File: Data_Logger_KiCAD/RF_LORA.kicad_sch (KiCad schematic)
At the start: 14 parts, among them U3 SX1262IMLTRT, U4 MASW-007221, Y2 Crystal_GND23

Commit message: Sub-schematics Generated
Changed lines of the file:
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@@
+	)
+	(junction
+		(at 83.82 38.1)
+		(diameter 0)
+		(color 0 0 0 0)
 	)
 	(junction
@@
 	(wire
 		(pts
+			(xy 83.82 29.21) (xy 83.82 38.1)
+		)
+		(stroke
+			(width 0)
+			(type default)
+		)
+	)
+	(wire
+		(pts
 			(xy 116.84 69.85) (xy 116.84 76.2)
 		)
@@
 	(wire
 		(pts
+			(xy 77.47 38.1) (xy 83.82 38.1)
+		)
+		(stroke
+			(width 0)
+			(type default)
+		)
+	)
+	(wire
+		(pts
 			(xy 71.12 104.14) (xy 83.82 104.14)
 		)
@@
 	(wire
 		(pts
-			(xy 96.52 38.1) (xy 77.47 38.1)
+			(xy 96.52 38.1) (xy 83.82 38.1)
 		)
 		(stroke
@@
 					(unit 1)
 				)
+			)
+		)
+	)
+	(symbol
+		(lib_id "power:VDDA")
+		(at 83.82 29.21 0)
+		(unit 1)
+		(exclude_from_sim no)
+		(in_bom yes)
+		(on_board yes)
+		(dnp no)
+		(fields_autoplaced yes)
+		(property "Reference" "#PWR024"
+			(at 83.82 33.02 0)
+			(effects
+				(font
+					(size 1.27 1.27)
+				)
+				(hide yes)
+			)
+		)
+		(property "Value" "VDD_Radio"
+			(at 83.82 25.4 0)
+			(effects
+				(font
+					(size 1.27 1.27)
+				)
+			)
+		)
+		(property "Footprint" ""
+			(at 83.82 29.21 0)
+			(effects
+				(font
+					(size 1.27 1.27)
+				)
+				(hide yes)
+			)
+		)
+		(property "Datasheet" ""
+			(at 83.82 29.21 0)
+			(effects
+				(font
+					(size 1.27 1.27)
+				)
+				(hide yes)
+			)
+		)
+		(property "Description" "Power symbol creates a global label with name \"VDDA\""
+			(at 83.82 29.21 0)
+			(effects
+				(font
+					(size 1.27 1.27)
+				)
+				(hide yes)
+			)
+		)
+		(pin "1"
+		)
+		(instances
+			(project ""
+				(path "/db968e42-3ace-4cc9-9096-9d8f48135c40/f67abaa3-07d9-44aa-9d82-6b11f8890146"
+					(reference "#PWR024")
+					(unit 1)
+				)

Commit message: Radio Layout V1.0
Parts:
- removed Y2: Crystal_GND23, symbol Device:Crystal_GND23
- added Y3: Crystal_GND24, Crystal:Crystal_SMD_2520-4Pin_2.5x2.0mm, symbol Device:Crystal_GND24
- C10: value 100n -> 47p; footprint (none) -> Capacitor_SMD:C_0402_1005Metric
- C11, C12, C7: footprint (none) -> Capacitor_SMD:C_0402_1005Metric
- C8: value 100n -> 1u; footprint (none) -> Capacitor_SMD:C_0402_1005Metric
- C9: value 100n -> 47n; footprint (none) -> Capacitor_SMD:C_0402_1005Metric
- L3, L4: value L -> 47n; footprint (none) -> Inductor_SMD:L_CommonModeChoke_Coilcraft_0603USB
- R3, R4: footprint (none) -> Resistor_SMD:R_0402_1005Metric
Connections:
- net GND: now also Y3.1, Y3.2
- net at U3.3 (XTA): now also Y3.3
- net DIO3: no longer names the net of U3.6 (DIO3)
- net DIO3: now also Y3.4
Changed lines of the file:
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@@
+	)
+	(junction
+		(at 43.18 80.01)
+		(diameter 0)
+		(color 0 0 0 0)
 	)
 	(junction
@@
 	(wire
 		(pts
-			(xy 57.15 71.12) (xy 83.82 71.12)
+			(xy 48.26 86.36) (xy 83.82 86.36)
 		)
 		(stroke
@@
 	(wire
 		(pts
-			(xy 43.18 73.66) (xy 43.18 76.2)
+			(xy 48.26 73.66) (xy 48.26 86.36)
 		)
 		(stroke
@@
 	(wire
 		(pts
-			(xy 43.18 76.2) (xy 57.15 76.2)
-		)
-		(stroke
-			(width 0)
-			(type default)
-		)
-	)
-	(wire
-		(pts
 			(xy 140.97 83.82) (xy 147.32 83.82)
 		)
@@
 	(wire
 		(pts
-			(xy 43.18 66.04) (xy 43.18 63.5)
+			(xy 43.18 63.5) (xy 43.18 69.85)
 		)
 		(stroke
@@
 	(wire
 		(pts
-			(xy 71.12 86.36) (xy 83.82 86.36)
-		)
-		(stroke
-			(width 0)
-			(type default)
-		)
-	)
-	(wire
-		(pts
 			(xy 208.28 86.36) (xy 254 86.36)
 		)
@@
 	(wire
 		(pts
+			(xy 38.1 73.66) (xy 38.1 80.01)
+		)
+		(stroke
+			(width 0)
+			(type default)
+		)
+	)
+	(wire
+		(pts
 			(xy 167.64 83.82) (xy 187.96 83.82)
 		)
@@
 	(wire
 		(pts
-			(xy 57.15 71.12) (xy 57.15 76.2)
-		)
-		(stroke
-			(width 0)
-			(type default)
-		)
-	)
-	(wire
-		(pts
 			(xy 220.98 91.44) (xy 220.98 129.54)
 		)
@@
 	(wire
 		(pts
+			(xy 43.18 80.01) (xy 43.18 77.47)
+		)
+		(stroke
+			(width 0)
+			(type default)
+		)
+	)
+	(wire
+		(pts
 			(xy 133.35 53.34) (xy 133.35 55.88)
 		)
@@
 	(wire
 		(pts
+			(xy 43.18 80.01) (xy 43.18 82.55)
+		)
+		(stroke
+			(width 0)
+			(type default)
+		)
+	)
+	(wire
+		(pts
+			(xy 38.1 80.01) (xy 43.18 80.01)
+		)
+		(stroke
+			(width 0)
+			(type default)
+		)
+	)
+	(wire
+		(pts
 			(xy 208.28 91.44) (xy 220.98 91.44)
 		)
@@
 			(width 0)
 			(type default)
-		)
-	)
-	(hierarchical_label "DIO3"
-		(shape input)
-		(at 71.12 86.36 180)
-		(effects
-			(font
-				(size 1.27 1.27)
-			)
-			(justify right)
 		)
 	)
@@
 	)
 	(hierarchical_label "MISO"
-		(shape input)
+		(shape output)
 		(at 71.12 99.06 180)
 		(effects
@@
 	)
 	(symbol
+		(lib_id "power:GND")
+		(at 43.18 82.55 0)
+		(unit 1)
+		(exclude_from_sim no)
+		(in_bom yes)
+		(on_board yes)
+		(dnp no)
+		(fields_autoplaced yes)
+		(property "Reference" "#PWR07"
+			(at 43.18 88.9 0)
+			(effects
+				(font
+					(size 1.27 1.27)
+				)
+				(hide yes)
+			)
+		)
+		(property "Value" "GND"
+			(at 43.18 87.63 0)
+			(effects
+				(font
+					(size 1.27 1.27)
+				)
+				(hide yes)
+			)
+		)
+		(property "Footprint" ""
+			(at 43.18 82.55 0)
+			(effects
+				(font
+					(size 1.27 1.27)
+				)
+				(hide yes)
+			)
+		)
+		(property "Datasheet" ""
+			(at 43.18 82.55 0)
+			(effects
+				(font
+					(size 1.27 1.27)
+				)
+				(hide yes)
+			)
+		)
+		(property "Description" "Power symbol creates a global label with name \"GND\" , ground"
+			(at 43.18 82.55 0)
+			(effects
+				(font
+					(size 1.27 1.27)
+				)
+				(hide yes)
+			)
+		)
+		(pin "1"
+		)
+		(instances
+			(project "Data_Logger_Board"
+				(path "/db968e42-3ace-4cc9-9096-9d8f48135c40/f67abaa3-07d9-44aa-9d82-6b11f8890146"
+					(reference "#PWR07")
+					(unit 1)
+				)
+			)
+		)
+	)
+	(symbol
 		(lib_id "Device:R")
 		(at 196.85 129.54 90)
@@
 			)
 		)
-		(property "Footprint" ""
+		(property "Footprint" "Resistor_SMD:R_0402_1005Metric"
 			(at 196.85 131.318 90)
 			(effects
@@
 	)
 	(symbol
+		(lib_id "Device:Crystal_GND24")
+		(at 43.18 73.66 90)
+		(unit 1)
+		(exclude_from_sim no)
+		(in_bom yes)
+		(on_board yes)
+		(dnp no)
+		(fields_autoplaced yes)
+		(property "Reference" "Y3"
+			(at 55.88 68.7068 90)
+			(effects
+				(font
+					(size 1.27 1.27)
+				)
+			)
+		)
+		(property "Value" "Crystal_GND24"
+			(at 55.88 71.2468 90)
+			(effects
+				(font
+					(size 1.27 1.27)
+				)
+			)
+		)
+		(property "Footprint" "Crystal:Crystal_SMD_2520-4Pin_2.5x2.0mm"
+			(at 43.18 73.66 0)
+			(effects
+				(font
+					(size 1.27 1.27)
+				)
+				(hide yes)
+			)
+		)
+		(property "Datasheet" "~"
+			(at 43.18 73.66 0)
+			(effects
+				(font
+					(size 1.27 1.27)
+				)
+				(hide yes)
+			)
+		)
+		(property "Description" "Four pin crystal, GND on pins 2 and 4"
+			(at 43.18 73.66 0)
+			(effects
+				(font
+					(size 1.27 1.27)
+				)
+				(hide yes)
+			)
+		)
+		(pin "4"
+		)
+		(pin "2"
+		)
+		(pin "1"
+		)
+		(pin "3"
+		)
+		(instances
+			(project ""
+				(path "/db968e42-3ace-4cc9-9096-9d8f48135c40/f67abaa3-07d9-44aa-9d82-6b11f8890146"
+					(reference "Y3")
+					(unit 1)
+				)
+			)
+		)
+	)
+	(symbol
 		(lib_id "power:VDDA")
 		(at 83.82 29.21 0)
@@
 			)
 		)
-		(property "Value" "L"
+		(property "Value" "47n"
 			(at 124.46 63.5 90)
 			(effects
@@
 			)
 		)
-		(property "Footprint" ""
+		(property "Footprint" "Inductor_SMD:L_CommonModeChoke_Coilcraft_0603USB"
 			(at 124.46 66.04 0)
 			(effects
@@
 			)
 		)
-		(property "Value" "L"
+		(property "Value" "47n"
 			(at 142.24 81.2799 0)
 			(effects
@@
 			)
 		)
-		(property "Footprint" ""
+		(property "Footprint" "Inductor_SMD:L_CommonModeChoke_Coilcraft_0603USB"
 			(at 140.97 80.01 0)
 			(effects
@@
 			)
 		)
-		(property "Footprint" ""
+		(property "Footprint" "Capacitor_SMD:C_0402_1005Metric"
 			(at 204.1652 121.92 0)
 			(effects
@@
 			)
 		)
-		(property "Footprint" ""
+		(property "Footprint" "Resistor_SMD:R_0402_1005Metric"
 			(at 196.85 114.808 90)
 			(effects
@@
 			)
 		)
-		(property "Value" "100n"
+		(property "Value" "47n"
 			(at 124.46 76.1999 0)
 			(effects
@@
 			)
 		)
-		(property "Footprint" ""
+		(property "Footprint" "Capacitor_SMD:C_0402_1005Metric"
 			(at 121.6152 78.74 0)
 			(effects
@@
 				(path "/db968e42-3ace-4cc9-9096-9d8f48135c40/f67abaa3-07d9-44aa-9d82-6b11f8890146"
 					(reference "C9")
-					(unit 1)
-				)
-			)
-		)
-	)
-	(symbol
-		(lib_id "Device:Crystal_GND23")
-		(at 43.18 69.85 90)
-		(unit 1)
-		(exclude_from_sim no)
-		(in_bom yes)
-		(on_board yes)
-		(dnp no)
-		(property "Reference" "Y2"
-			(at 43.18 61.976 90)
-			(effects
-				(font
-					(size 1.27 1.27)
-				)
-			)
-		)
-		(property "Value" "Crystal_GND23"
-			(at 43.18 64.77 90)
-			(effects
-				(font
-					(size 1.27 1.27)
-				)
-			)
-		)
-		(property "Footprint" ""
-			(at 43.18 69.85 0)
-			(effects
-				(font
-					(size 1.27 1.27)
-				)
-				(hide yes)
-			)
-		)
-		(property "Datasheet" "~"
-			(at 43.18 69.85 0)
-			(effects
-				(font
-					(size 1.27 1.27)
-				)
-				(hide yes)
-			)
-		)
-		(property "Description" "Four pin crystal, GND on pins 2 and 3"
-			(at 43.18 69.85 0)
-			(effects
-				(font
-					(size 1.27 1.27)
-				)
-				(hide yes)
-			)
-		)
-		(pin "4"
-		)
-		(pin "1"
-		)
-		(pin "3"
-		)
-		(pin "2"
-		)
-		(instances
-			(project "Data_Logger_Board"
-				(path "/db968e42-3ace-4cc9-9096-9d8f48135c40/f67abaa3-07d9-44aa-9d82-6b11f8890146"
-					(reference "Y2")
 					(unit 1)
 				)
@@
 			)
 		)
-		(property "Value" "100n"
+		(property "Value" "47p"
 			(at 135.89 76.1999 0)
 			(effects
@@
 			)
 		)
-		(property "Footprint" ""
+		(property "Footprint" "Capacitor_SMD:C_0402_1005Metric"
 			(at 133.0452 78.74 0)
 			(effects
@@
 			)
 		)
-		(property "Value" "100n"
+		(property "Value" "1u"
 			(at 137.16 60.9599 0)
 			(effects
@@
 			)
 		)
-		(property "Footprint" ""
+		(property "Footprint" "Capacitor_SMD:C_0402_1005Metric"
 			(at 134.3152 63.5 0)
 			(effects
@@
 			)
 		)
-		(property "Footprint" ""
+		(property "Footprint" "Capacitor_SMD:C_0402_1005Metric"
 			(at 112.7252 46.99 0)
 			(effects
@@
 			)
 		)
-		(property "Footprint" ""
+		(property "Footprint" "Capacitor_SMD:C_0402_1005Metric"
 			(at 204.1652 138.43 0)
 			(effects

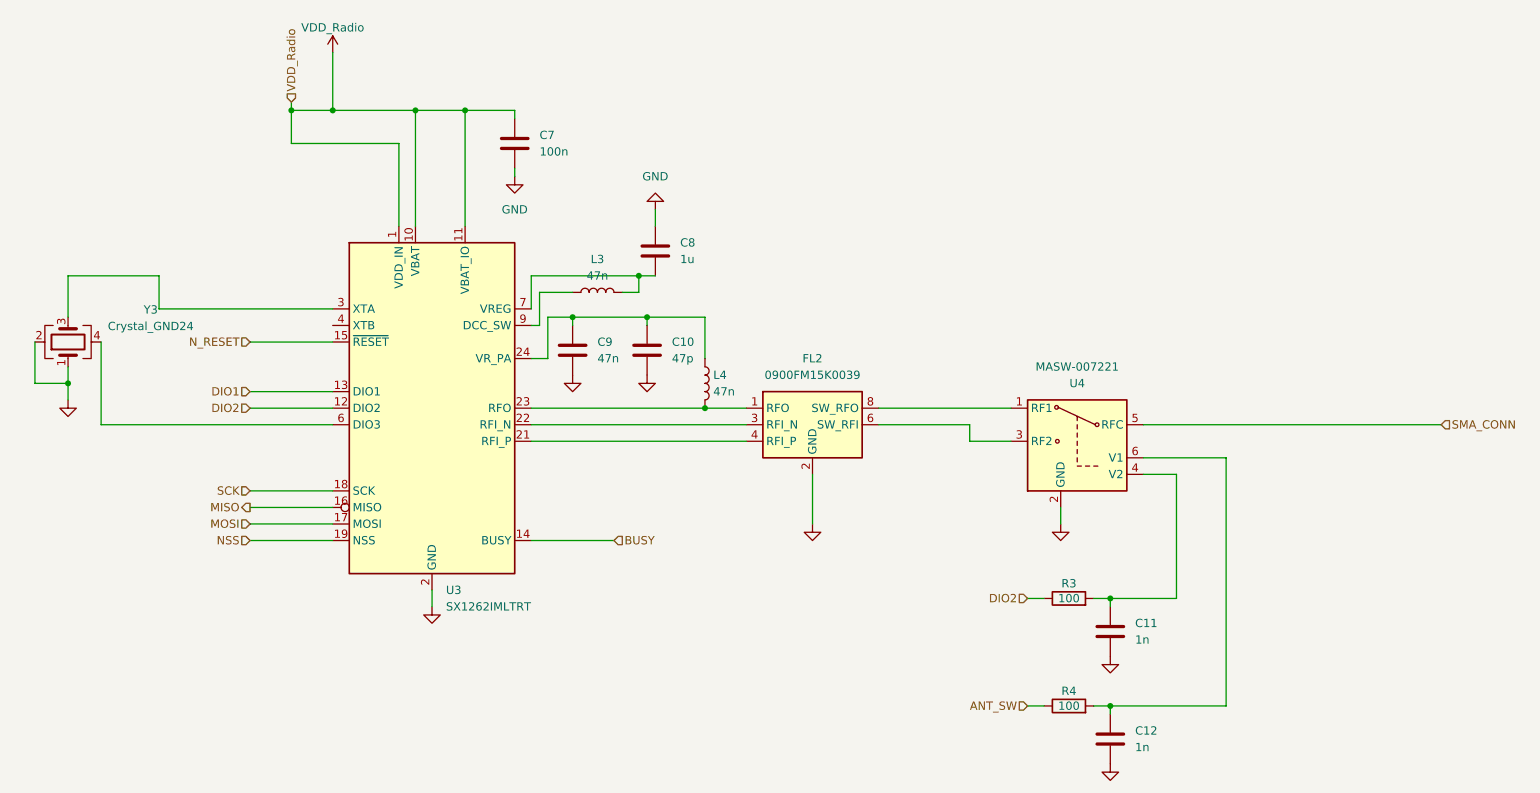
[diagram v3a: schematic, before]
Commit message: Aggregated sub schematics into single primary schematic
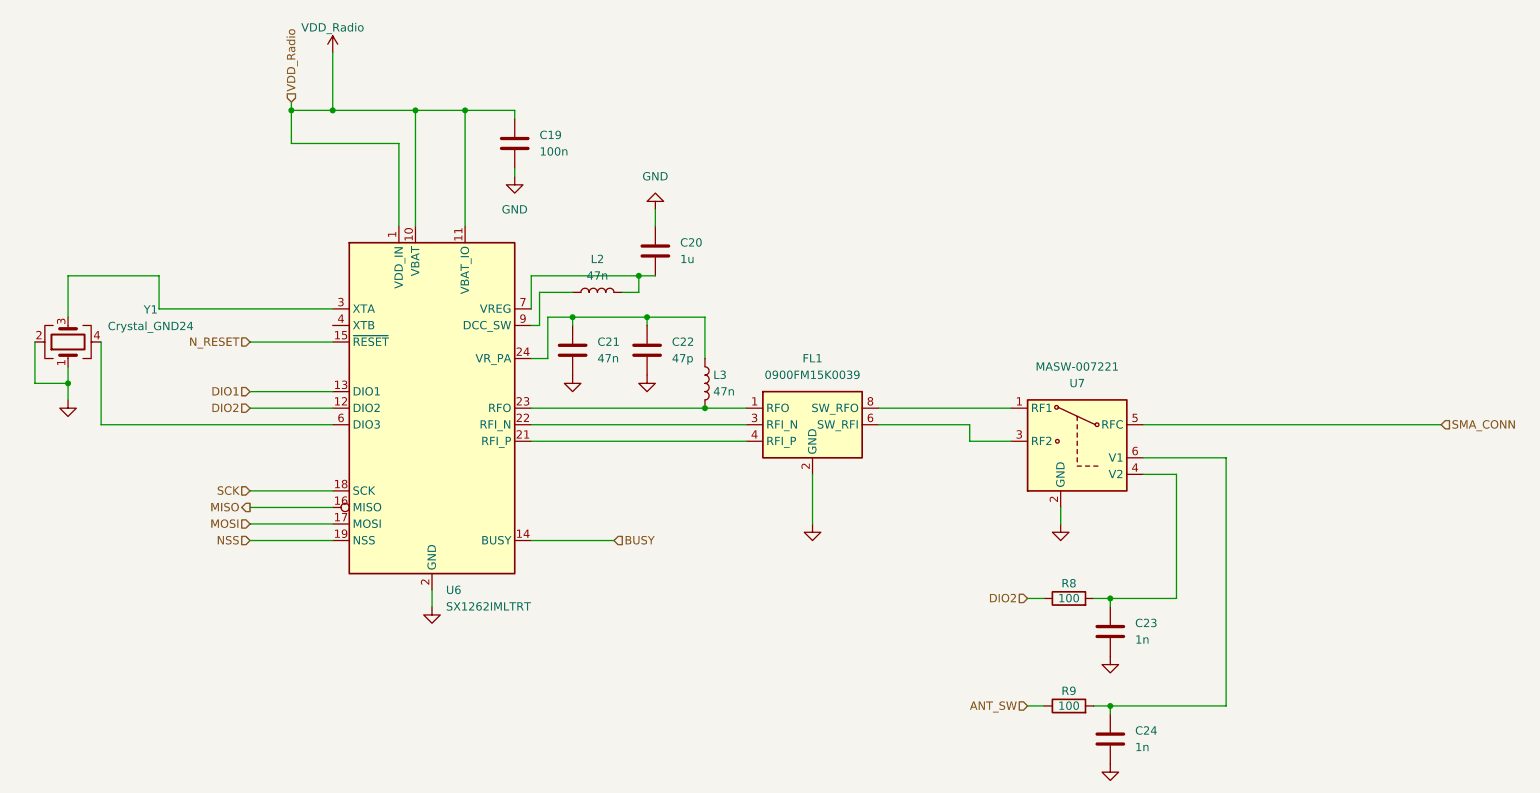
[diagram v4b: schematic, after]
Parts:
- renumbered C7 to C19, C8 to C20, C9 to C21, C10 to C22, C11 to C23, C12 to C24, FL2 to FL1, L3 to L2, L4 to L3, R3 to R8, R4 to R9, U3 to U6, U4 to U7, Y3 to Y1
